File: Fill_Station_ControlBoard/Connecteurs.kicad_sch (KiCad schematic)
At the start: 60 parts, among them J3 USB_C_Receptacle_USB2.0_14P, J6 RJ45_Wuerth_7499010211A, J8 DE9_Socket_MountingHoles, U2 USBLC6-2SC6, U3 TCAN337G, U5 LAN8742A

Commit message: Modifs de l'organisation des pages
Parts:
- removed C11, C35: 10n, Capacitor_SMD:C_0603_1608Metric, symbol Device:C
- removed C36, C7: 10uF, Capacitor_SMD:C_0603_1608Metric, symbol Device:C
- removed C37: 100nF, Capacitor_SMD:C_0603_1608Metric, symbol Device:C
- removed C38: 1uF, Capacitor_SMD:C_0603_1608Metric, symbol Device:C
- removed C40, C41, C44, C50: ~, Capacitor_SMD:C_0603_1608Metric, symbol Device:C
- removed C42, C43: 22u, Capacitor_SMD:C_0603_1608Metric, symbol Device:C
- removed C6: 0.1uF, Capacitor_SMD:C_0603_1608Metric, symbol Device:C
- removed C87: 0.1u, Capacitor_SMD:C_0603_1608Metric, symbol Device:C
- removed D1: ESDA5V3L, Package_TO_SOT_SMD:SOT-23-3, symbol Power_Protection:ESDA5V3L
- removed D3: 6.4V, symbol Device:D_Zener
- removed F3: Polyfuse, symbol Device:Polyfuse
- removed J3: USB_C_Receptacle_USB2.0_14P, Connector_USB:USB_C_Receptacle_Amphenol_12401548E4-2A_CircularHoles, symbol Connector:USB_C_Receptacle_USB2.0_14P
- removed J8: DE9_Socket_MountingHoles, Connector_Dsub:DSUB-9_Socket_Vertical_P2.77x2.84mm_MountingHoles, symbol Connector:DE9_Socket_MountingHoles
- removed R3, R4: 5.1k, Resistor_SMD:R_0603_1608Metric_Pad0.98x0.95mm_HandSolder, symbol Device:R_US
- removed R41: 100, Resistor_SMD:R_0603_1608Metric_Pad0.98x0.95mm_HandSolder, symbol Device:R_US
- removed R42, R43: 33, Resistor_SMD:R_0603_1608Metric_Pad0.98x0.95mm_HandSolder, symbol Device:R_US
- removed R44: 120, Resistor_SMD:R_0603_1608Metric_Pad0.98x0.95mm_HandSolder, symbol Device:R_US
- removed R46: 10k, Resistor_SMD:R_0603_1608Metric_Pad0.98x0.95mm_HandSolder, symbol Device:R_US
- removed R48: 0, Resistor_SMD:R_0603_1608Metric_Pad0.98x0.95mm_HandSolder, symbol Device:R_US
- removed R5: *, Resistor_SMD:R_0603_1608Metric_Pad0.98x0.95mm_HandSolder, symbol Device:R_US
- removed U2: USBLC6-2SC6, Package_TO_SOT_SMD:SOT-23-6, symbol Power_Protection:USBLC6-2SC6
- removed U3: TCAN337G, Package_TO_SOT_SMD:TSOT-23-8_HandSoldering, symbol Interface_CAN_LIN:TCAN337G
- added R10, R11: 49.9, Capacitor_SMD:C_0603_1608Metric, symbol Device:R_US
- C39: value 22u -> 1nF
- C51: value ~ -> 100n
- R6, R7: value 60 -> 49.9
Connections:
- net 3V3: now also C39.1, C51.1, J6.4 (CTD), J6.5 (CRD), R6.1, R7.1, R10.1, R11.1
- net GND: no longer C39.2, J6.8
- net TX_N: now also R7.2
- net TX_P: now also R6.2
- net RX_N: now reaches J6.6 (RD-), U5.22 (RXN)
- net RX_N: now also R11.2
- net RX_P: now reaches J6.3 (RD+), U5.23 (RXP)
- net RX_P: now also R10.2
- net CHASSIS: now reaches J6.SH
- net CHASSIS: now also C39.2, J6.8
- net Eth.CLKIN: no longer names the net of U5.5 (XTAL1/CLKIN)
- no-connect marks 5 -> 1
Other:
- note removed: "CAN"
- note removed: "Ces trois condo doivent être près des cotés inputs des I/O Valeurs trouvé selon une fréquence de 1MHz"
- note removed: "DNI"
- note removed: "Deux condos près du connecteur"
- note removed: "Option: ajouter tvs protection (TPD4E02B04)"
- note removed: "Placer esd très proche du port"
- note removed: "Pull up de TXD seulement si STM est à drain ouvert"
- note removed: "USBC"
- note removed: "pull up?"
- moved on the sheet: C10, C12, C13, C28, C29, C30, C51, C9, J6, L1, R17, R18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

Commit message: Ajout power
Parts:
- added R36: 33, Resistor_SMD:R_0603_1608Metric_Pad0.98x0.95mm_HandSolder, symbol Device:R_US
- added R37: 270, Resistor_SMD:R_0603_1608Metric_Pad0.98x0.95mm_HandSolder, symbol Device:R_US
- C12: value ~ -> 1u
- C13: value ~ -> 100n
- R26: value 2.5k -> 1k
- R28: value 33 -> 10k
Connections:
- net Eth.RXER is gone; now on net GND: R28.1
- net Eth.REFCLKO: now also R36.1; no longer U5.14 (~{INT}/REFCLKO)
- net GND: now also R37.2
- net LED2: now also R37.1
- new net: R36.2, U5.14 (~{INT}/REFCLKO)
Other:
- note removed: "25Mhz clock"
- moved on the sheet: R30, R8

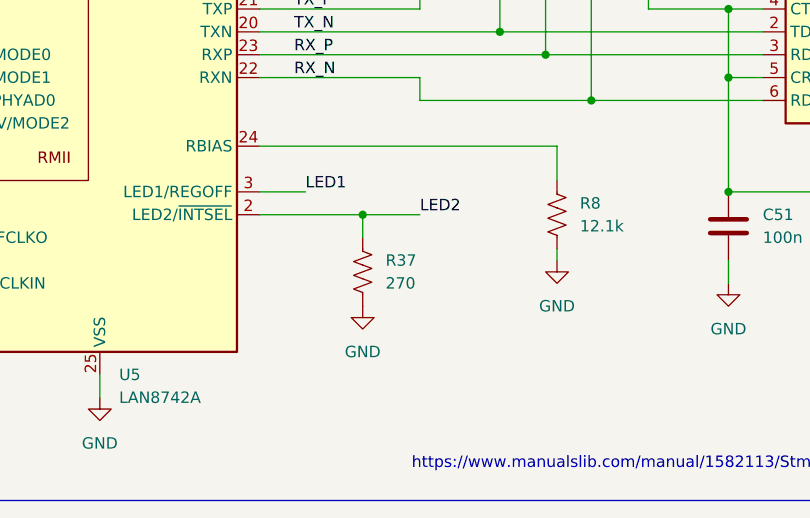
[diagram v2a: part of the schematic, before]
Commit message: Changement val Resistance a 10k
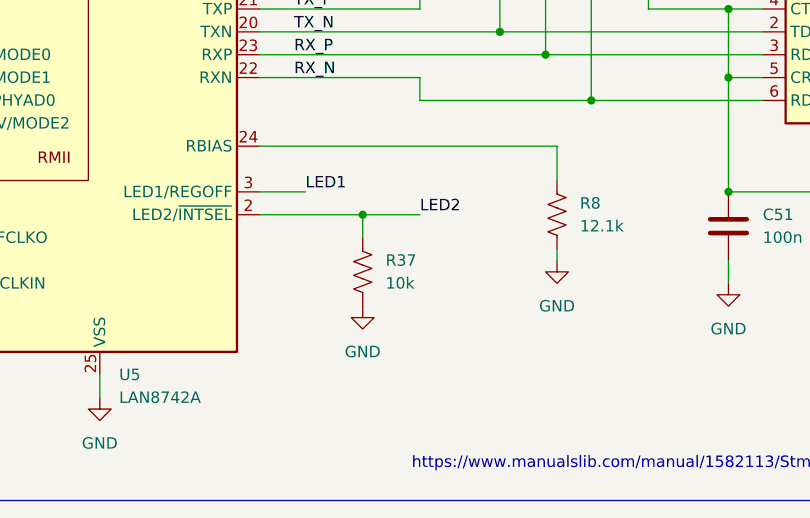
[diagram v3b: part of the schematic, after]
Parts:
- R37: value 270 -> 10k
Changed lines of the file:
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@@
 			)
 		)
-		(property "Value" "270"
+		(property "Value" "10k"
 			(at 215.9 162.5599 0)
 			(effects

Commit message: début layout
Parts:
- removed C30: ~, Capacitor_SMD:C_0603_1608Metric, symbol Device:C
- removed C39: 1nF, Capacitor_SMD:C_0603_1608Metric, symbol Device:C
- removed R10, R11: 49.9, Capacitor_SMD:C_0603_1608Metric, symbol Device:R_US
- removed R6, R7: 49.9, Resistor_SMD:R_0603_1608Metric_Pad0.98x0.95mm_HandSolder, symbol Device:R_US
- added C5: 10u, Capacitor_SMD:C_0603_1608Metric, symbol Device:C
- added C8: 100n, Capacitor_SMD:C_0603_1608Metric, symbol Device:C
- added R14, R16: 10k, Resistor_SMD:R_0603_1608Metric_Pad0.98x0.95mm_HandSolder, symbol Device:R_US
- added R18, R20, R21, R22: 49.9, Resistor_SMD:R_0603_1608Metric_Pad0.98x0.95mm_HandSolder, symbol Device:R_US
- C6: renamed from C28; value ~ -> 10u
- C7: renamed from C29; value ~ -> 100n
- R1: renamed from R24; value 33 -> 22
- R17: renamed from R37; now not fitted
- R2: value 33 -> 22
- R3: renamed from R36; value 33 -> 22
- R4: renamed from R21; value 33 -> 22
- R6: renamed from R22; value 33 -> 22
- R7: renamed from R25; value 33 -> 22
- R8: renamed from R23; value 33 -> 22
- renumbered C12 to C1, C9 to C2, C10 to C3, C13 to C4, C51 to C9, J6 to J1, R32 to R10, R33 to R11, R26 to R12, R17 to R13, R30 to R15, R8 to R19, R18 to R23, R19 to R24, R28 to R5, R31 to R9, U5 to U1
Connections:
- net 3V3: now also C5.1, R14.1; no longer C9.1, J1.4 (CTD), J1.5 (CRD)
- net CHASSIS: no longer J1.8
- net GND: now also C5.2, C8.2, R16.2
- net LED1: now also R16.1
- net RX_N: now also R22.2
- net RX_P: now also R21.2
- net TX_N: now also R20.2
- net TX_P: now also R18.2
- net at R3.2, U1.14 (~{INT}/REFCLKO): now also R14.2
- net 3V3A: now reaches C6.1, C7.1, L1.2, U1.1 (VDD2A), U1.19 (VDD1A)
- net 3V3A: now also C9.1, J1.4 (CTD), J1.5 (CRD), C8.1, R18.1, R20.1, R21.1, R22.1
- net Clock25Mhz: now reaches U1.5 (XTAL1/CLKIN)
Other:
- moved on the sheet: C1, C2, C3, C4, C6, C7, C9, J1, L1, R1, R10, R11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

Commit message: PCB fait
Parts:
- added C15: 100n, Capacitor_SMD:C_0402_1005Metric, symbol Device:C
- added C71: 1000p - 2000V, Capacitor_SMD:C_1210_3225Metric, symbol Device:C
- added C84: 10u, Capacitor_SMD:C_0402_1005Metric, symbol Device:C
- added C85: *, Capacitor_SMD:C_0402_1005Metric, symbol Device:C
- added R57: 10k, Capacitor_SMD:C_0402_1005Metric, symbol Device:R_US
- added R58: 0, Capacitor_SMD:C_0402_1005Metric, symbol Device:R_US
- added R83: 1M, Resistor_SMD:R_0603_1608Metric_Pad0.98x0.95mm_HandSolder, symbol Device:R_US
- added Y3: ASV-25.000MHz, Oscillator:Oscillator_SMD_Abracon_ASV-4Pin_7.0x5.1mm, symbol Oscillator:ASV-xxxMHz
- C7, C8: footprint Capacitor_SMD:C_0603_1608Metric -> Resistor_SMD:R_0402_1005Metric
- C9: footprint Capacitor_SMD:C_0603_1608Metric -> Capacitor_SMD:C_0402_1005Metric
- L1: footprint (none) -> Capacitor_SMD:C_0402_1005Metric
- R1, R19, R2, R3, R4, R6, R7, R8: footprint Resistor_SMD:R_0603_1608Metric_Pad0.98x0.95mm_HandSolder -> Resistor_SMD:R_0402_1005Metric
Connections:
- net CHASSIS is gone; now on net CHASSIS_ETH: J1.SH
- net 3V3: now also C15.1, C84.1, R57.1, Y3.4 (Vdd)
- net GND: now also C15.2, C71.1, C84.2, C85.2, R83.1, Y3.2 (GND)
- net TXD_N: now reaches R4.2, U1.18 (TXD1)
- net TXD_P: now reaches R2.2, U1.17 (TXD0)
- net CHASSIS_ETH: now reaches J1.8
- net CHASSIS_ETH: now also C71.2, R83.2
- net 3V3A renamed 3V3A_Eth
- net Clock25Mhz renamed Eth_Clock_25Mhz
- net Eth_Clock_25Mhz: now also C85.1, R58.2
- new net: R57.2, Y3.1 (EN)
- new net: R58.1, Y3.3 (OUT)
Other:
- moved on the sheet: C9, R2, R4

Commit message: Travail Layout
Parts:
- removed C1: 1u, Capacitor_SMD:C_0603_1608Metric, symbol Device:C
- removed C15, C9: 100n, Capacitor_SMD:C_0402_1005Metric, symbol Device:C
- removed C2: 1uF, Capacitor_SMD:C_0603_1608Metric, symbol Device:C
- removed C3: 470pF, Capacitor_SMD:C_0603_1608Metric, symbol Device:C
- removed C4: 100n, Capacitor_SMD:C_0603_1608Metric, symbol Device:C
- removed C5, C6: 10u, Capacitor_SMD:C_0603_1608Metric, symbol Device:C
- removed C7, C8: 100n, Resistor_SMD:R_0402_1005Metric, symbol Device:C
- removed C71: 1000p - 2000V, Capacitor_SMD:C_1210_3225Metric, symbol Device:C
- removed C84: 10u, Capacitor_SMD:C_0402_1005Metric, symbol Device:C
- removed C85: *, Capacitor_SMD:C_0402_1005Metric, symbol Device:C
- removed J1: RJ45_Wuerth_7499010211A, Connector_RJ:RJ45_Wuerth_7499010211A_Horizontal, symbol Connector:RJ45_Wuerth_7499010211A
- removed L1: L_Ferrite, Capacitor_SMD:C_0402_1005Metric, symbol Device:L_Ferrite
- removed R10, R11, R13, R14, R15, R16, R17, R5, R9: 10k, Resistor_SMD:R_0603_1608Metric_Pad0.98x0.95mm_HandSolder, symbol Device:R_US
- removed R12: 1k, Resistor_SMD:R_0603_1608Metric_Pad0.98x0.95mm_HandSolder, symbol Device:R_US
- removed R18, R20, R21, R22: 49.9, Resistor_SMD:R_0603_1608Metric_Pad0.98x0.95mm_HandSolder, symbol Device:R_US
- removed R19: 12.1k, Resistor_SMD:R_0402_1005Metric, symbol Device:R_US
- removed R2, R3, R4, R6, R7, R8: 22, Resistor_SMD:R_0402_1005Metric, symbol Device:R_US
- removed R23, R24: 270, Resistor_SMD:R_0603_1608Metric_Pad0.98x0.95mm_HandSolder, symbol Device:R_US
- removed R57: 10k, Capacitor_SMD:C_0402_1005Metric, symbol Device:R_US
- removed R58: 0, Capacitor_SMD:C_0402_1005Metric, symbol Device:R_US
- removed R83: 1M, Resistor_SMD:R_0603_1608Metric_Pad0.98x0.95mm_HandSolder, symbol Device:R_US
- removed U1: LAN8742A, Package_DFN_QFN:VQFN-24-1EP_4x4mm_P0.5mm_EP2.5x2.5mm_ThermalVias, symbol Interface_Ethernet:LAN8742A
- removed Y3: ASV-25.000MHz, Oscillator:Oscillator_SMD_Abracon_ASV-4Pin_7.0x5.1mm, symbol Oscillator:ASV-xxxMHz
- added C100, C101: 10u, Capacitor_SMD:C_0603_1608Metric, symbol Device:C
- added C102, C97: 1u, Capacitor_SMD:C_0603_1608Metric, symbol Device:C
- added C103, C92, C94, C98: 100n, Capacitor_SMD:C_0402_1005Metric, symbol Device:C
- added C104, C99: 10n, Capacitor_SMD:C_0402_1005Metric, symbol Device:C
- added C105, C93: 1000p - 2000V, Capacitor_SMD:C_1210_3225Metric, symbol Device:C
- added C95: 10u, Capacitor_SMD:C_0402_1005Metric, symbol Device:C
- added C96: *, Capacitor_SMD:C_0402_1005Metric, symbol Device:C
- added J1: RJ45_Wuerth_74980111211, Connector_RJ:RJ45_Wuerth_74980111211_Horizontal, symbol Connector:RJ45_Wuerth_74980111211
- added L4: L_Ferrite, Capacitor_SMD:C_0402_1005Metric, symbol Device:L_Ferrite
- added R101, R104, R115, R116: 22, Resistor_SMD:R_0402_1005Metric, symbol Device:R_US
- added R102: 6.49k, Resistor_SMD:R_0402_1005Metric, symbol Device:R_US
- added R106: 1M, Resistor_SMD:R_0603_1608Metric_Pad0.98x0.95mm_HandSolder, symbol Device:R_US
- added R107: 270, Resistor_SMD:R_0603_1608Metric_Pad0.98x0.95mm_HandSolder, symbol Device:R_US
- added R111: 10k, Capacitor_SMD:C_0402_1005Metric, symbol Device:R_US
- added R112: 0, Capacitor_SMD:C_0402_1005Metric, symbol Device:R_US
- added R117, R118, R119, R120: 10k, Resistor_SMD:R_0603_1608Metric_Pad0.98x0.95mm_HandSolder, symbol Device:R_US
- added U5: DP83825I, Package_DFN_QFN:Texas_RMQ0024A_WQFN-24-1EP_3x3mm_P0.4mm_EP1.9x1.9mm, symbol Interface_Ethernet:DP83825I
- added Y4: ASV-25.000MHz, Oscillator:Oscillator_SMD_Abracon_ASV-4Pin_7.0x5.1mm, symbol Oscillator:ASV-xxxMHz
- R1: value 22 -> 10k; footprint Resistor_SMD:R_0402_1005Metric -> Resistor_SMD:R_0603_1608Metric_Pad0.98x0.95mm_HandSolder
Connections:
- net Eth.RXD1 is gone; now on net 3V3: R1.1
- net 3V3: now also C100.1, C94.1, C95.1, C97.1, C98.1, C99.1, L4.2, R107.1, R111.1, R117.1, U5.19 (VDDIO), Y4.4 (Vdd)
- net CHASSIS_ETH: now also C105.2, C93.2, J1.10, J1.SH, R106.2
- net Eth.CRS_DV: now also R104.1, R119.1
- net Eth.MDC: now also U5.16 (MDC)
- net Eth.MDIO: now also U5.15 (MDIO)
- net Eth.REFCLKO: now also R101.1
- net Eth.RST: now also R1.2, U5.5 (~{RST})
- net Eth.TXEN: now also U5.1 (TX_EN)
- net Eth_Clock_25Mhz: now also C96.1, R112.2, U5.13 (XI/50MHzIn)
- net GND: now also C100.2, C101.2, C102.2, C103.2, C104.2, C105.1, C92.2, C93.1, C94.2, C95.2, C96.2, C97.2, C98.2, C99.2, R102.2, R106.1, R118.2, R119.2, R120.2, U5.21 (GND), U5.25 (GND), U5.9 (GND), Y4.2 (GND)
- net RX_N: now also J1.8 (RD-), U5.7 (RD-)
- net RX_P: now also J1.6 (RD+), U5.8 (RD+)
- net TX_N: now also J1.5 (TD-), U5.10 (TD-)
- net TX_P: now also J1.3 (TD+), U5.11 (TD+)
- new net: C101.1, C102.1, C103.1, C104.1, L4.1, U5.6 (VDDA3V3)
- new net: R111.2, Y4.1 (EN)
- new net: R112.1, Y4.3 (OUT)
- new net: J1.12, R107.2
- new net: C92.1, J1.4 (TCT), J1.7 (RCT)
- new net: R101.2, U5.2 (50MHzOut/LED2/S(RX_DV_EN))
- new net: R102.1, U5.14 (RBIAS)
- new net: R117.2, U5.3 (INTR/~{PWRDN})
- new net CRS_DV: R104.2, U5.20 (CRS_DV/S(PhyAdd[1]))
- new net Eth.RXD_N: R116.1
- new net Eth.RXD_P: R115.1, R120.1
- new net Eth.TXD_N: U5.24 (TX_D1)
- new net Eth.TXD_P: U5.23 (TX_D0)
- new net LED0: J1.11, R118.1, U5.4 (LED0/S(ANEG_Dis))
- new net RXD_N: R116.2, U5.17 (RX_D1/S(Master/Slave))
- new net RXD_P: R115.2, U5.18 (RX_D0/S(PhyAdd[0]))
- no-connect marks 1 -> 2
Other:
- note added: "7.2.2.1 RMII Layout Guidelines 1. Remember that RMII signals as single-ended signals. 2. Traces must be routed with 50Ω impedance to ground. 3. Keep trace lengths as short as possible. TI recommends to keep the trace lengths between two to six inches long."
- note added: "7.2.2.2 MDI Layout Guidelines 1. Remember that MDI signals are differential. 2. Traces must be routed with 50Ω impedance to ground and 100Ω differential controlled impedance. 3. Route MDI traces to the transformer on the same layer. 4. Use a metal-shielded RJ-45 connector and electrically connect the shield to chassis ground. 5. Avoid supplies and ground beneath the magnetics. 6. Do not overlap t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"
- note removed: "C'est normal que la pin VDDCR n'est pas alimenté - mettre les cap très proche de la chip"
- note removed: "Phy Ethernet - RMII"
- note removed: "https://www.manualslib.com/manual/1582113/Stmicroelectronics-Stm32h7-Nucleo-144.html?page=29"

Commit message: PCB presque terminé
Modifs de l'alim
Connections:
- no-connect marks 2 -> 4
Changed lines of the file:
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@@
+	)
+	(no_connect
+		(at 312.42 107.95)
 	)
 	(no_connect
 		(at 152.4 161.29)
+	)
+	(no_connect
+		(at 312.42 105.41)
 	)
 	(wire
@@
 		(effects
 			(font
-				(size 1.27 1.27)
-			)
-			(justify left bottom)
-		)
-	)
-	(label "TXEN"
-		(at 144.78 107.95 0)
-		(effects
-			(font

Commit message: Final_V1
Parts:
- C100, C101: LCSC (none) -> C22399626
- C102, C97: LCSC (none) -> C59302
- C103, C92, C94, C98: LCSC (none) -> C60474
- C104, C99: LCSC (none) -> C3850633
- C105, C93: LCSC (none) -> C9196
- C95: footprint Capacitor_SMD:C_0402_1005Metric -> Capacitor_SMD:C_0603_1608Metric; LCSC (none) -> C22399626
- C96, R106: now left out of the parts list
- J1: LCSC (none) -> C5523973
- L4: footprint Capacitor_SMD:C_0402_1005Metric -> Resistor_SMD:R_0402_1005Metric; LCSC (none) -> C160977
- R1, R117, R118: footprint Resistor_SMD:R_0603_1608Metric_Pad0.98x0.95mm_HandSolder -> Resistor_SMD:R_0603_1608Metric; LCSC (none) -> C22369937
- R101, R104, R115, R116: LCSC (none) -> C25092
- R102: LCSC (none) -> C25916
- R107: value 270 -> 680; LCSC (none) -> C22356475
- R111: footprint Capacitor_SMD:C_0402_1005Metric -> Resistor_SMD:R_0402_1005Metric; LCSC (none) -> C173683
- R112: footprint Capacitor_SMD:C_0402_1005Metric -> Resistor_SMD:R_0402_1005Metric; LCSC (none) -> C17168
- R119, R120: footprint Resistor_SMD:R_0603_1608Metric_Pad0.98x0.95mm_HandSolder -> Resistor_SMD:R_0603_1608Metric
- U5: LCSC (none) -> C783599
- Y4: LCSC (none) -> C1987509
